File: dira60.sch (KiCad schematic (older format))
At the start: 20 parts, among them J0 USB_C_Receptacle, SW0 RESET, U0 ATmega32U4-AU, X0 XTAL_GND

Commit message: Schematic updated
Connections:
- net D-: now reaches J0.A7 (D-), J0.B7 (D-), U0.3 (D-)
- net D+: now reaches J0.A6 (D+), J0.B6 (D+), U0.4 (D+)
- no-connect marks 0 -> 11
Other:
- moved on the sheet: C10, C3, C4, C5, C6, C9, R0, R1, SW0, X0

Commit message: Updated Schematic
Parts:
- added R5, R6: 22, symbol Device:R_Small
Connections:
- net D+: now also R6.1; no longer J0.A6 (D+), J0.B6 (D+)
- net D-: now also R5.1; no longer J0.A7 (D-), J0.B7 (D-)
- new net: J0.A6 (D+), J0.B6 (D+), R6.2
- new net: J0.A7 (D-), J0.B7 (D-), R5.2
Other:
- moved on the sheet: C0, C1, C10, C2, C3, C4, C5, C6, C7, C8, C9, J0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

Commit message: Basic Schema complete
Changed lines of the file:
@@
 EESchema Schematic File Version 4
+LIBS:dira60-cache
 EELAYER 26 0
 EELAYER END
 $Descr A4 11693 8268
 encoding utf-8
-Sheet 1 1
+Sheet 1 2
 Title ""
 Date ""
@@
 Wire Wire Line
 	3250 2400 3050 2400
+$Sheet
+S 13700 -200 4200 1650
+U 5C3ADE7A
+F0 "Matrix" 50
+F1 "file5C3ADE79.sch" 50
+$EndSheet
 $EndSCHEMATC

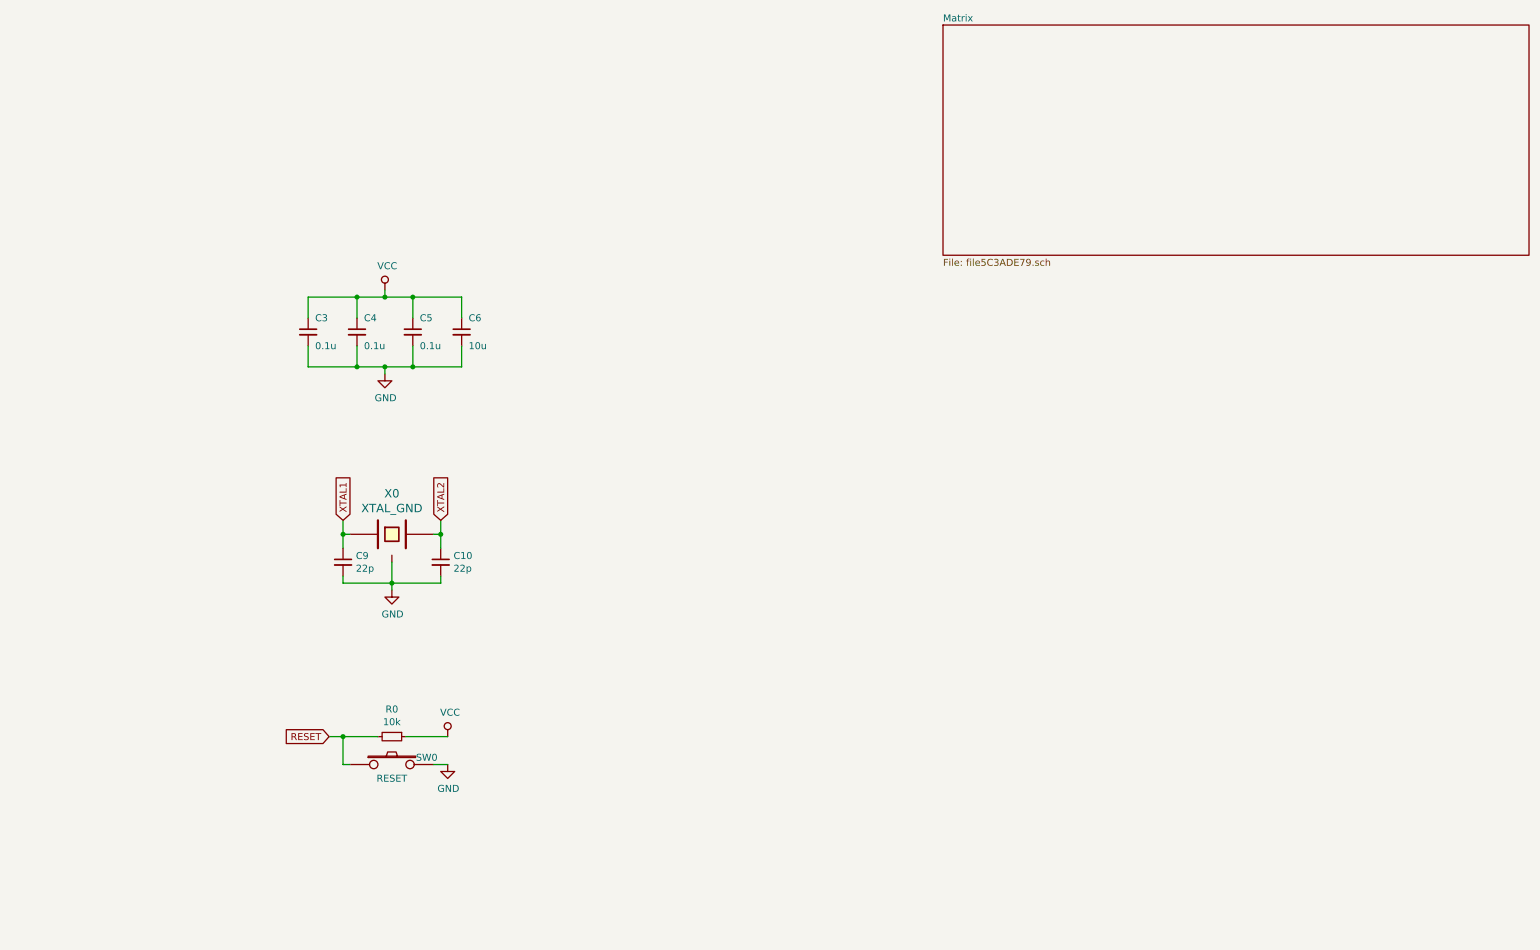
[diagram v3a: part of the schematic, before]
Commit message: Added Submodules
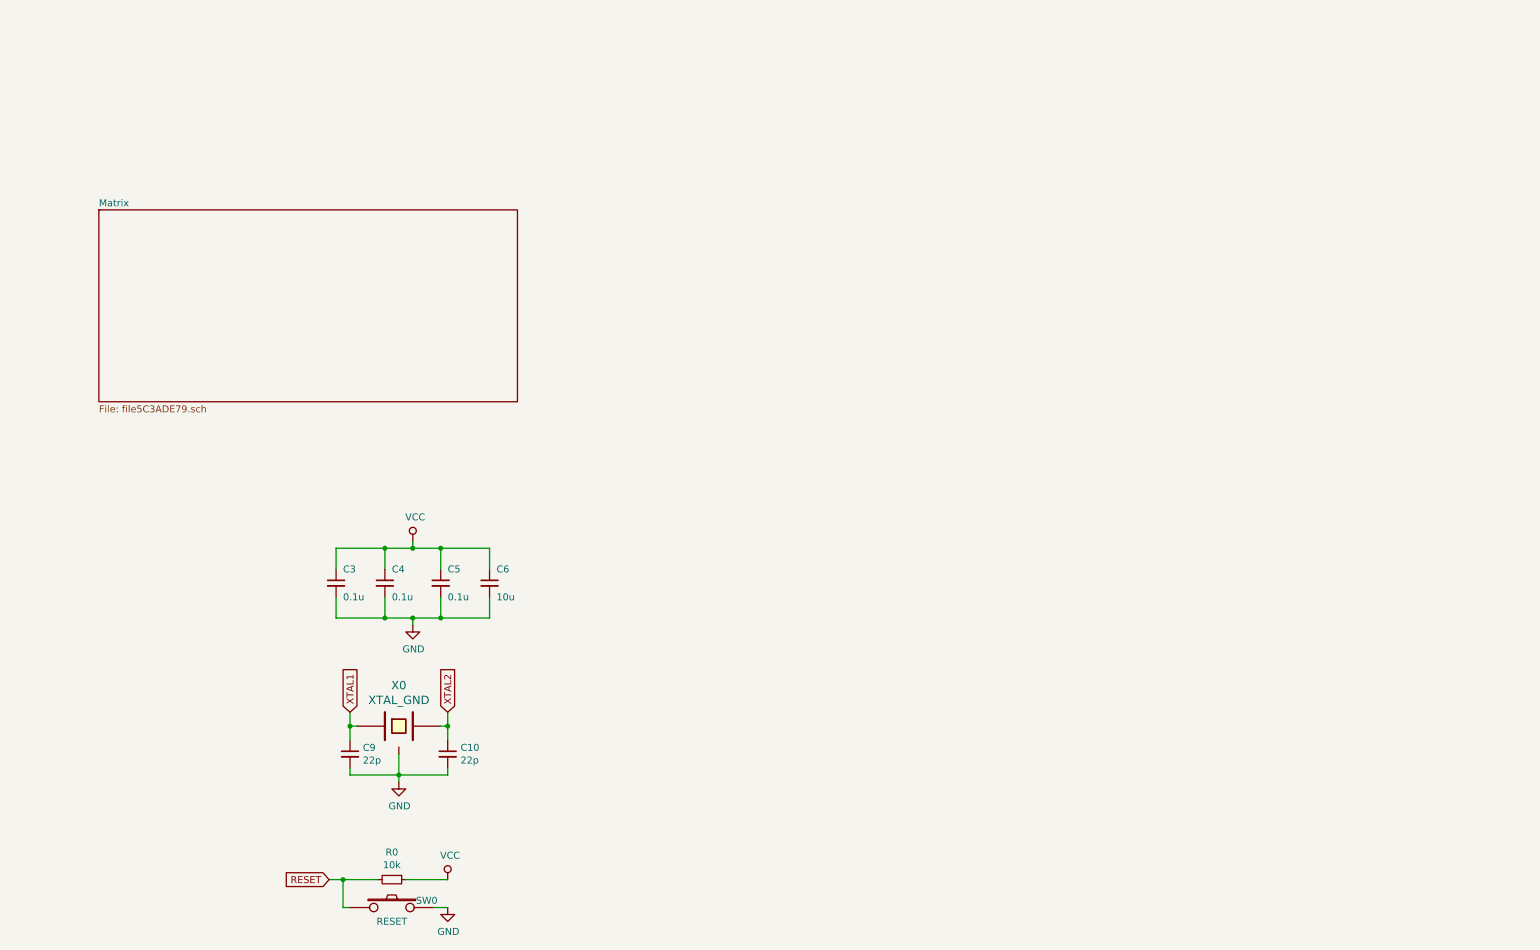
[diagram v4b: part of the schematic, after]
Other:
- moved on the sheet: C10, C3, C4, C5, C6, C9, R0, SW0, X0

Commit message: Generated Netlist
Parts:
- C0, C1, C10, C2, C3, C4, C5, C6, C7, C8, C9: footprint (none) -> Capacitor_SMD:C_0805_2012Metric_Pad1.15x1.40mm_HandSolder
- J0: footprint (none) -> Type-C:HRO-TYPE-C-31-M-12-HandSoldering
- R0, R1, R2, R3, R4, R5, R6: footprint (none) -> Resistor_SMD:R_0805_2012Metric_Pad1.15x1.40mm_HandSolder
- SW0: footprint (none) -> random-keyboard-parts:SKQG-1155865
- X0: footprint (none) -> Crystal:Crystal_SMD_3225-4Pin_3.2x2.5mm
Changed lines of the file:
@@
 F 0 "R0" V 9554 5925 50  0000 C CNN
 F 1 "10k" V 9645 5925 50  0000 C CNN
-F 2 "" H 9750 5925 50  0001 C CNN
+F 2 "Resistor_SMD:R_0805_2012Metric_Pad1.15x1.40mm_HandSolder" H 9750 5925 50  0001 C CNN
 F 3 "~" H 9750 5925 50  0001 C CNN
 	1    9750 5925
@@
 F 0 "SW0" H 10000 6175 50  0000 C CNN
 F 1 "RESET" H 9750 6025 50  0000 C CNN
-F 2 "" H 9750 6125 60  0000 C CNN
+F 2 "random-keyboard-parts:SKQG-1155865" H 9750 6125 60  0001 C CNN
 F 3 "" H 9750 6125 60  0000 C CNN
 	1    9750 6125
@@
 F 0 "J0" H 2005 3967 50  0000 C CNN
 F 1 "USB_C_Receptacle" H 2005 3876 50  0000 C CNN
-F 2 "" H 2050 2700 50  0001 C CNN
+F 2 "Type-C:HRO-TYPE-C-31-M-12-HandSoldering" H 2050 2700 50  0001 C CNN
 F 3 "https://www.usb.org/sites/default/files/documents/usb_type-c.zip" H 2050 2700 50  0001 C CNN
 	1    1900 2700
@@
 F 0 "C0" H 3942 1246 50  0000 L CNN
 F 1 "4.7u" H 3942 1155 50  0000 L CNN
-F 2 "" H 3850 1200 50  0001 C CNN
+F 2 "Capacitor_SMD:C_0805_2012Metric_Pad1.15x1.40mm_HandSolder" H 3850 1200 50  0001 C CNN
 F 3 "~" H 3850 1200 50  0001 C CNN
 	1    3850 1200
@@
 F 0 "R2" V 2650 2050 50  0000 C CNN
 F 1 "5.1k" V 2700 1900 50  0000 C CNN
-F 2 "" H 2700 1900 50  0001 C CNN
+F 2 "Resistor_SMD:R_0805_2012Metric_Pad1.15x1.40mm_HandSolder" H 2700 1900 50  0001 C CNN
 F 3 "~" H 2700 1900 50  0001 C CNN
 	1    2700 1900
@@
 F 0 "R3" V 2650 2150 50  0000 C CNN
 F 1 "5.1k" V 2700 2000 50  0000 C CNN
-F 2 "" H 2700 2000 50  0001 C CNN
+F 2 "Resistor_SMD:R_0805_2012Metric_Pad1.15x1.40mm_HandSolder" H 2700 2000 50  0001 C CNN
 F 3 "~" H 2700 2000 50  0001 C CNN
 	1    2700 2000
@@
 F 0 "C7" V 4550 3050 50  0000 C CNN
 F 1 "1u" V 4750 3050 50  0000 C CNN
-F 2 "" H 4650 3050 50  0001 C CNN
+F 2 "Capacitor_SMD:C_0805_2012Metric_Pad1.15x1.40mm_HandSolder" H 4650 3050 50  0001 C CNN
 F 3 "~" H 4650 3050 50  0001 C CNN
 	1    4650 3050
@@
 F 0 "C8" V 1521 4500 50  0000 C CNN
 F 1 "4.7n" V 1612 4500 50  0000 C CNN
-F 2 "" H 1750 4500 50  0001 C CNN
+F 2 "Capacitor_SMD:C_0805_2012Metric_Pad1.15x1.40mm_HandSolder" H 1750 4500 50  0001 C CNN
 F 3 "~" H 1750 4500 50  0001 C CNN
 	1    1750 4500
@@
 F 0 "R4" V 1850 4650 50  0000 C CNN
 F 1 "1M" V 1750 4650 50  0000 C CNN
-F 2 "" H 1750 4650 50  0001 C CNN
+F 2 "Resistor_SMD:R_0805_2012Metric_Pad1.15x1.40mm_HandSolder" H 1750 4650 50  0001 C CNN
 F 3 "~" H 1750 4650 50  0001 C CNN
 	1    1750 4650
@@
 F 0 "C1" H 5550 1150 50  0000 L CNN
 F 1 "0.1u" H 5500 1050 50  0000 L CNN
-F 2 "" H 5500 1100 50  0001 C CNN
+F 2 "Capacitor_SMD:C_0805_2012Metric_Pad1.15x1.40mm_HandSolder" H 5500 1100 50  0001 C CNN
 F 3 "~" H 5500 1100 50  0001 C CNN
 	1    5500 1100
@@
 F 0 "C2" V 5850 1250 50  0000 C CNN
 F 1 "0.1u" V 6050 1250 50  0000 C CNN
-F 2 "" H 5950 1250 50  0001 C CNN
+F 2 "Capacitor_SMD:C_0805_2012Metric_Pad1.15x1.40mm_HandSolder" H 5950 1250 50  0001 C CNN
 F 3 "~" H 5950 1250 50  0001 C CNN
 	1    5950 1250
@@
 F 0 "R1" V 6300 3850 50  0000 C CNN
 F 1 "10k" V 6400 3850 50  0000 C CNN
-F 2 "" H 6400 3850 50  0001 C CNN
+F 2 "Resistor_SMD:R_0805_2012Metric_Pad1.15x1.40mm_HandSolder" H 6400 3850 50  0001 C CNN
 F 3 "~" H 6400 3850 50  0001 C CNN
 	1    6400 3850
@@
 F 0 "X0" H 9800 5117 60  0000 C CNN
 F 1 "XTAL_GND" H 9800 5011 60  0000 C CNN
-F 2 "" H 9800 4825 60  0000 C CNN
+F 2 "Crystal:Crystal_SMD_3225-4Pin_3.2x2.5mm" H 9800 4825 60  0001 C CNN
 F 3 "" H 9800 4825 60  0000 C CNN
 	1    9800 4825
@@
 F 0 "C9" H 9542 5071 50  0000 L CNN
 F 1 "22p" H 9542 4980 50  0000 L CNN
-F 2 "" H 9450 5025 50  0001 C CNN
+F 2 "Capacitor_SMD:C_0805_2012Metric_Pad1.15x1.40mm_HandSolder" H 9450 5025 50  0001 C CNN
 F 3 "~" H 9450 5025 50  0001 C CNN
 	1    9450 5025
@@
 F 0 "C10" H 10242 5071 50  0000 L CNN
 F 1 "22p" H 10242 4980 50  0000 L CNN
-F 2 "" H 10150 5025 50  0001 C CNN
+F 2 "Capacitor_SMD:C_0805_2012Metric_Pad1.15x1.40mm_HandSolder" H 10150 5025 50  0001 C CNN
 F 3 "~" H 10150 5025 50  0001 C CNN
 	1    10150 5025
@@
 F 0 "C3" H 9400 3900 50  0000 L CNN
 F 1 "0.1u" H 9400 3700 50  0000 L CNN
-F 2 "" H 9350 3800 50  0001 C CNN
+F 2 "Capacitor_SMD:C_0805_2012Metric_Pad1.15x1.40mm_HandSolder" H 9350 3800 50  0001 C CNN
 F 3 "~" H 9350 3800 50  0001 C CNN
 	1    9350 3800
@@
 F 0 "C4" H 9750 3900 50  0000 L CNN
 F 1 "0.1u" H 9750 3700 50  0000 L CNN
-F 2 "" H 9700 3800 50  0001 C CNN
+F 2 "Capacitor_SMD:C_0805_2012Metric_Pad1.15x1.40mm_HandSolder" H 9700 3800 50  0001 C CNN
 F 3 "~" H 9700 3800 50  0001 C CNN
 	1    9700 3800
@@
 F 0 "C5" H 10150 3900 50  0000 L CNN
 F 1 "0.1u" H 10150 3700 50  0000 L CNN
-F 2 "" H 10100 3800 50  0001 C CNN
+F 2 "Capacitor_SMD:C_0805_2012Metric_Pad1.15x1.40mm_HandSolder" H 10100 3800 50  0001 C CNN
 F 3 "~" H 10100 3800 50  0001 C CNN
 	1    10100 3800
@@
 F 0 "C6" H 10500 3900 50  0000 L CNN
 F 1 "10u" H 10500 3700 50  0000 L CNN
-F 2 "" H 10450 3800 50  0001 C CNN
+F 2 "Capacitor_SMD:C_0805_2012Metric_Pad1.15x1.40mm_HandSolder" H 10450 3800 50  0001 C CNN
 F 3 "~" H 10450 3800 50  0001 C CNN
 	1    10450 3800
@@
 F 0 "R5" V 2900 2350 50  0000 C CNN
 F 1 "22" V 2950 2200 50  0000 C CNN
-F 2 "" H 2950 2200 50  0001 C CNN
+F 2 "Resistor_SMD:R_0805_2012Metric_Pad1.15x1.40mm_HandSolder" H 2950 2200 50  0001 C CNN
 F 3 "~" H 2950 2200 50  0001 C CNN
 	1    2950 2200
@@
 F 0 "R6" V 2900 2550 50  0000 C CNN
 F 1 "22" V 2950 2400 50  0000 C CNN
-F 2 "" H 2950 2400 50  0001 C CNN
+F 2 "Resistor_SMD:R_0805_2012Metric_Pad1.15x1.40mm_HandSolder" H 2950 2400 50  0001 C CNN
 F 3 "~" H 2950 2400 50  0001 C CNN
 	1    2950 2400

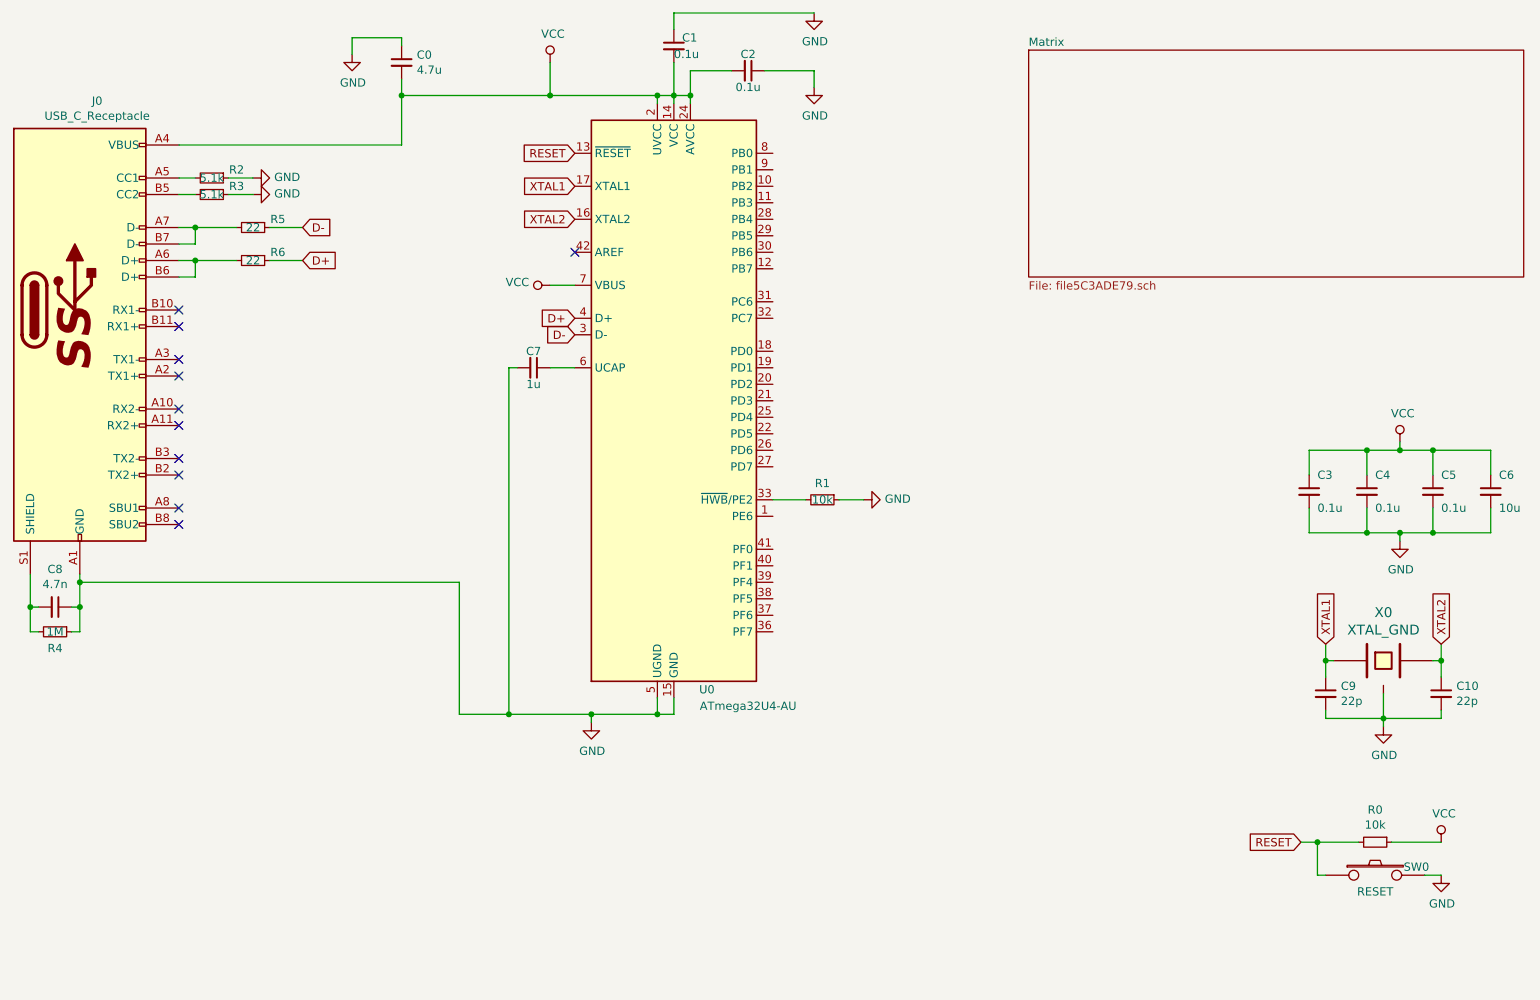
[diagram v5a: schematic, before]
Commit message: Added type C
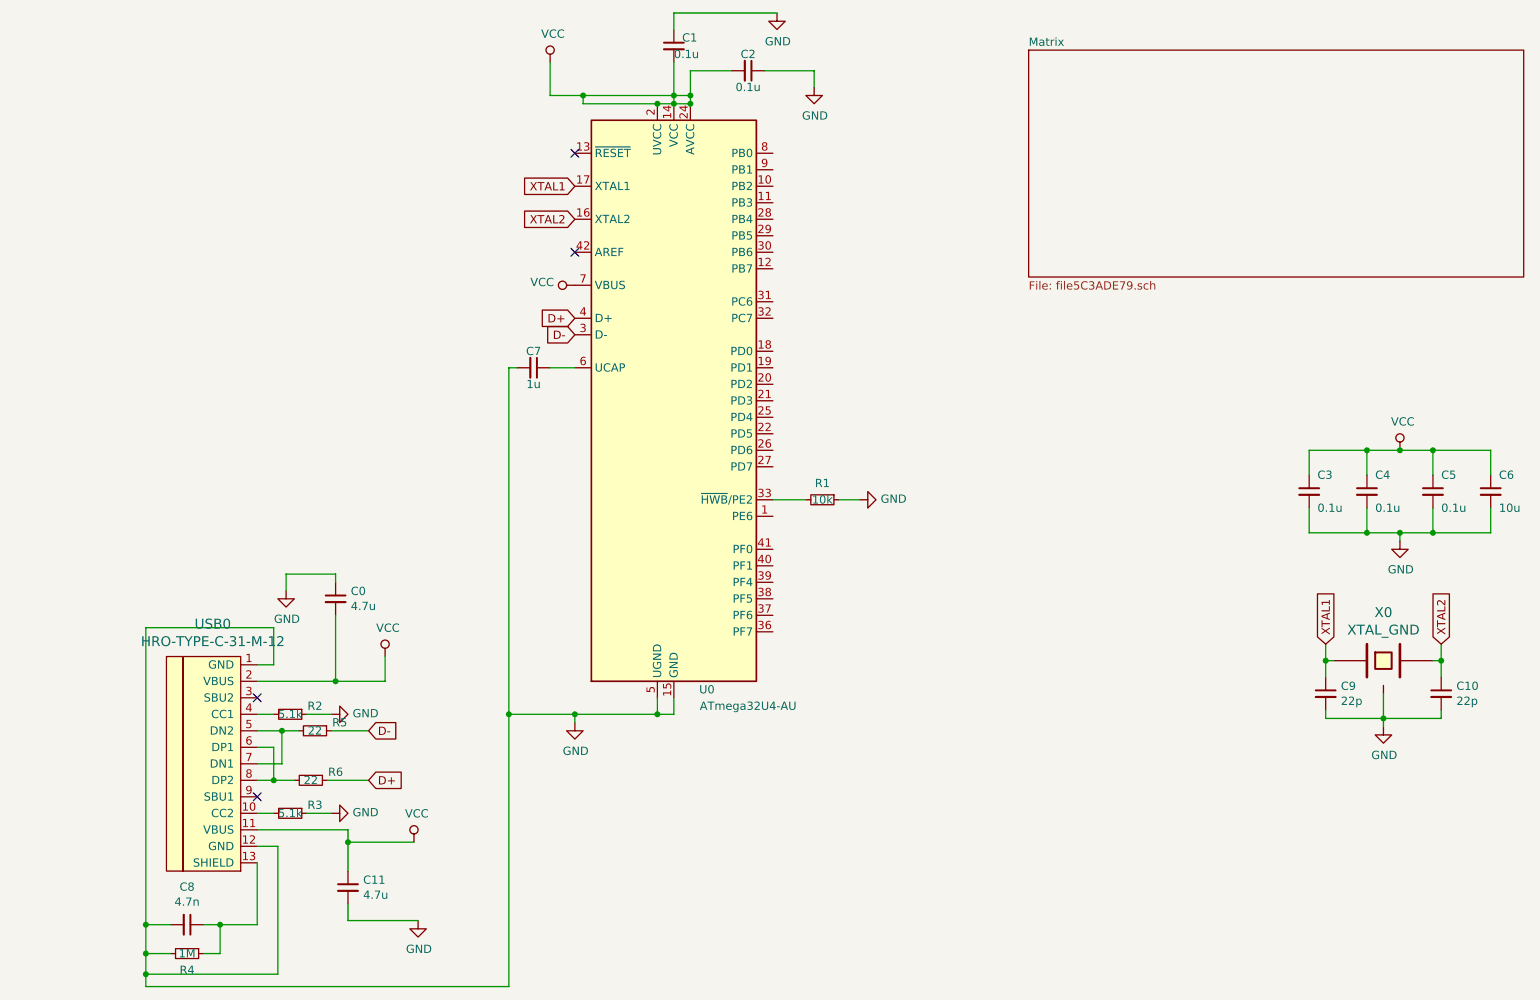
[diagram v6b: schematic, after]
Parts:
- removed J0: USB_C_Receptacle, Type-C:HRO-TYPE-C-31-M-12-HandSoldering, symbol Connector:USB_C_Receptacle
- removed R0: 10k, Resistor_SMD:R_0805_2012Metric_Pad1.15x1.40mm_HandSolder, symbol Device:R_Small
- removed SW0: RESET, random-keyboard-parts:SKQG-1155865, symbol keyboard_parts:SW_PUSH
- added C11: 4.7u, Capacitor_SMD:C_0805_2012Metric_Pad1.15x1.40mm_HandSolder, symbol Device:C_Small
- added USB0: HRO-TYPE-C-31-M-12, Type-C:HRO-TYPE-C-31-M-12-HandSoldering, symbol Type-C:HRO-TYPE-C-31-M-12
- U0: footprint Package_QFP:TQFP-44_10x10mm_P0.8mm -> keyboard_parts:QFN-44-1EP_7x7mm_Pitch0.5mm
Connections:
- net GND: now also C8.2, R4.2, C11.2, USB0.1 (GND), USB0.12 (GND); no longer C8.1, R4.1
- net VCC: now also C11.1, USB0.11 (VBUS), USB0.2 (VBUS)
- net at R2.2: now also USB0.4 (CC1)
- net at R6.2: now also USB0.6 (DP1), USB0.8 (DP2)
- net at R5.2: now also USB0.5 (DN2), USB0.7 (DN1)
- net at R3.2: now also USB0.10 (CC2)
- net RESET: no longer names the net of U0.13 (~RESET)
- new net: C8.1, R4.1, USB0.13 (SHIELD)
- no-connect marks 11 -> 4
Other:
- moved on the sheet: C0, R2, R3
